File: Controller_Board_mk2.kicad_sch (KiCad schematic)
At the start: 31 parts, among them J1 Barrel_Jack_MountingPin, J2 Barrel_Jack_MountingPin, J3 Barrel_Jack_MountingPin, J4 Barrel_Jack_MountingPin, J5 Barrel_Jack_MountingPin, K1 SANYOU_SRD_Form_C, K2 SANYOU_SRD_Form_C, K3 SANYOU_SRD_Form_C, K4 SANYOU_SRD_Form_C, Q1 BC817, Q2 BC817, Q3 BC817, Q4 BC817, U1 AP63205WU

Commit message: Redid schematic and added fuse sensors
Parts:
- added F1, F2, F3, F4: RUILONSMD1812P050TF/30, Fuse:Fuse_1812_4532Metric, symbol Device:Polyfuse
- added Polyfuse: Littelfuse MINISMDC260F/16-2, Fuse:Fuse_1812_4532Metric, symbol Device:Polyfuse
- added R10, R11, R12, R9: 33k, Resistor_SMD:R_0603_1608Metric, symbol Device:R
- added R5, R6, R7, R8: 100k, Resistor_SMD:R_0603_1608Metric, symbol Device:R
- J1, J2, J3, J4, J5: footprint Connector_BarrelJack:BarrelJack_Wuerth_694108106102_2.5x5.5mm -> Connector_BarrelJack:BarrelJack_CUI_PJ-102AH_Horizontal
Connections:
- net GND: now also R10.2, R11.2, R12.2, R9.2
- net at D13.1 (K), D14.1 (K), D15.1 (K)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: now also F1.2, F2.2, F3.2, F4.2, R5.1, R6.1, R7.1, R8.1; no longer J1.1, U1.2 (EN), U1.3 (IN)
- net at D13.2 (A), J2.2: now also K4.4; no longer K4.3
- net at D16.2 (A), J5.2: now also K1.4; no longer K1.3
- net at D15.2 (A), J4.2: now also D14.2 (A), J3.2, K2.4, K3.4, F1.1, F2.1, F3.1, F4.1, Polyfuse.2; no longer K2.3
- net at A1.1 (GP0): now also R5.2, R9.1
- net at A1.2 (GP1): now also R10.1, R6.2
- net at A1.4 (GP2): now also R11.1, R7.2
- net at A1.5 (GP3): now also R12.1, R8.2
- new net: J1.1, Polyfuse.1, U1.2 (EN), U1.3 (IN)
- now unconnected: K3.3
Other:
- moved on the sheet: D13, D14, D15, D16, J2, J3, J4, J5

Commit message: routed mostly everything and fixed some minor errors
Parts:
- removed D10, D11, D12, D9: 1N4148W, Diode_SMD:D_SOD-123, symbol Diode:1N4148W
- added D1, D2, D3, D4: 1N4148W, Diode_SMD:D_SOD-123, symbol Diode:1N4148W
- renumbered Polyfuse to Polyfuse1
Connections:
- net GND: now also J1.2, K1.4, K2.4, K3.4, K4.4, Q1.2 (E), Q2.2 (E), Q3.2 (E), Q4.2 (E); no longer K1.5, K2.5, K3.5, K4.5
- net at R3.2: now also A1.11 (GP8); no longer A1.17 (GP13)
- net at D13.2 (A), J2.2: now also K4.1; no longer K4.4
- net at A1.39 (VSYS), C1.1, C2.1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: no longer Q1.3 (C), Q2.3 (C), Q3.3 (C), Q4.3 (C)
- net at K1.2: now also F1.1, F2.1, F3.1, F4.1, K2.2, K3.2, K4.2, Polyfuse1.2, D1.1 (K), D2.1 (K), D3.1 (K), D4.1 (K); no longer Q4.2 (E)
- net at D16.2 (A), J5.2: now also K1.1; no longer K1.4
- net at R2.2: now also A1.12 (GP9); no longer A1.19 (GP14)
- net at R1.1: now also A1.9 (GP6); no longer A1.20 (GP15)
- net at A1.10 (GP7): now also R4.2
- net at A1.16 (GP12): no longer R4.2
- new net: D13.1 (K), F2.2, J2.1, R5.1
- new net: D2.2 (A), K3.5, Q4.3 (C)
- new net: D4.2 (A), K1.5, Q2.3 (C)
- new net: D16.1 (K), F4.2, J5.1, R8.1
- new net: D15.1 (K), F3.2, J4.1, R7.1
- new net: D15.2 (A), J4.2, K2.1
- new net: D14.1 (K), F1.2, J3.1, R6.1
- new net: D14.2 (A), J3.2, K3.1
- new net: D3.2 (A), K2.5, Q3.3 (C)
- new net: D1.2 (A), K4.5, Q1.3 (C)
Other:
- moved on the sheet: D13, D14, D15, D16, F1, F2, F3, F4, J1, J2, J3, J4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

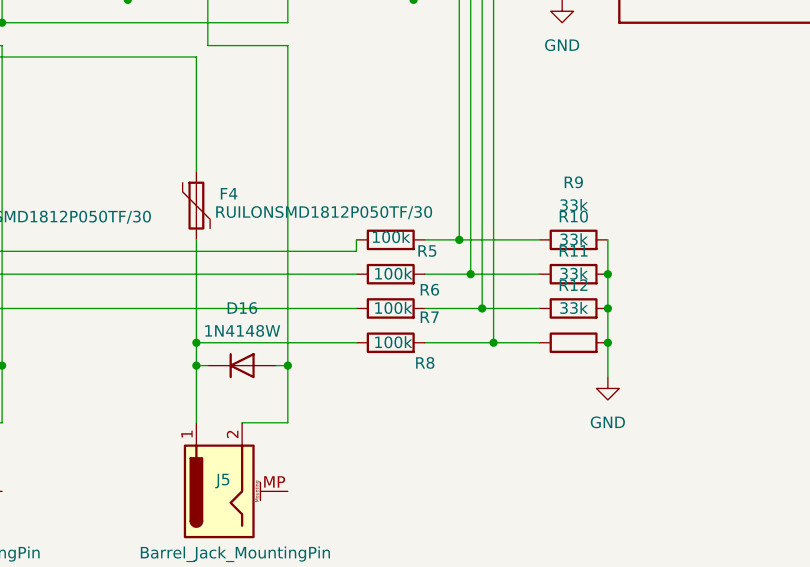
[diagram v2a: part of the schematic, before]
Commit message: added some LCSC part numbers in the schematic
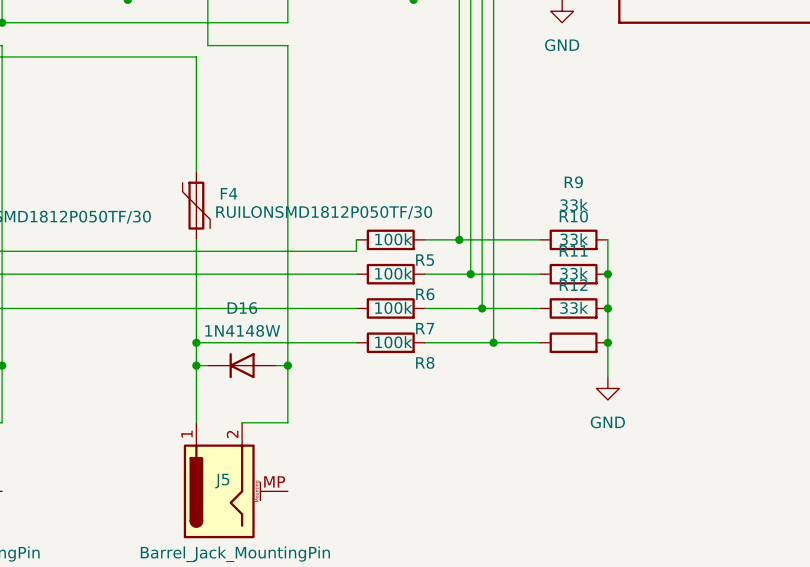
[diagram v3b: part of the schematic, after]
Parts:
- F1, F2, F3, F4: LCSC (none) -> C12559
- Polyfuse1: LCSC (none) -> C16490
- R10, R11, R12, R9: LCSC (none) -> C4216
- R5, R6, R7, R8: LCSC (none) -> C25803
